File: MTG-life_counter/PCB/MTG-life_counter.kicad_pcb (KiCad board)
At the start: 2 copper layers, 65 x 43 mm, 51 parts, among them J1 USB_C_Receptacle, J2 AVR-ISP-6, Q1 IRLML6244, Q2 Si2301DS, Q3 Si2301DS, SW1 SW_Push, SW2 SW_Push, U1 MCP73831-2-OT, U2 AT90S4433-8P, U3 HDSP-H101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

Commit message: USB C connector placed and routed.
This fixes #6.
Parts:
- added D3: S1B, Diode_SMD:D_SMA_Handsoldering, B.Cu at (123.5, 120.2)
- moved C4 41.3 mm to (125.5, 110.6), turned to 180 degrees
- moved D1 30.8 mm to (132.5, 110.6), turned to 0 degrees
- moved R16 23.8 mm to (139.2, 103.7)
- moved R20 23.0 mm to (139.2, 105.7)
- moved D2 20.6 mm to (145.0, 103.6), turned to 180 degrees
- moved REF** 17.8 mm to (160.3, 125.9)
- moved R13 17.2 mm to (143.7, 106.3), turned to 180 degrees
- moved J1 16.0 mm to (132.5, 106.5)
- moved REF** 15.4 mm to (149.4, 108.8)
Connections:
- net Net-(J1-PadA5) renamed /Power/CC1
- net Net-(J1-PadB5) renamed /Power/CC2
- J2 pad 2: +BATT -> Net-(D3-Pad2)
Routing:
- net /Power/VUSB: track 96.5 -> 67.3 mm
- net +BATT: track 92.3 -> 71.6 mm
- net /Power/CHARGER_STAT: track 43.1 -> 26.0 mm
- net /Power/CC1: track 0.00 -> 7.46 mm
- net /Power/CC2: track 0.00 -> 7.12 mm
- net GND: track 26.8 -> 33.3 mm
- net Net-(D3-Pad2): track 0.00 -> 5.96 mm
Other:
- board text added: "+BTN"
- board text added: "-BTN"
- board text added: "Battery"
- board text added: "Charging"
- board text added: "Rev. 22/2"
- board text removed: "Rev. 22/1"

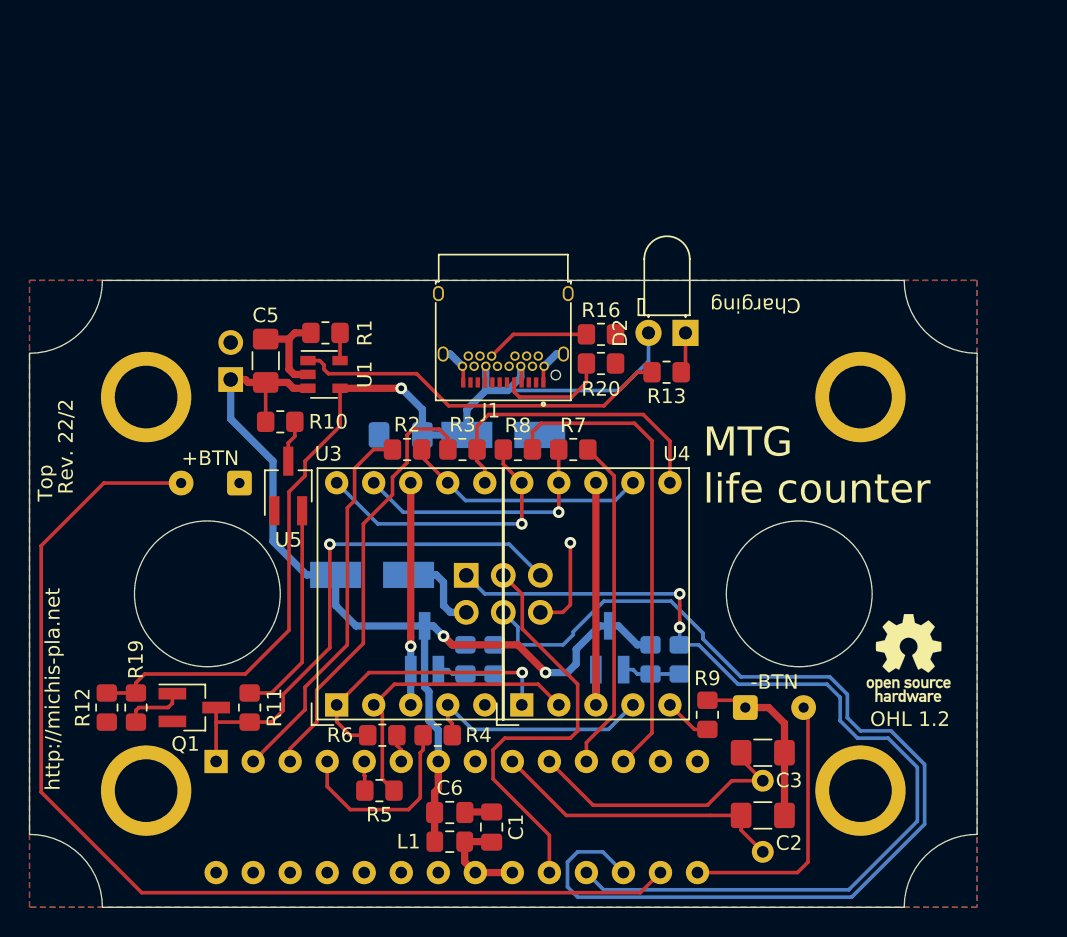
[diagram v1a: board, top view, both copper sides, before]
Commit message: Add an on/off switch. This fixes #7.
Also fix ERC errors, rename nets to indicate the signals logic level, move some components a bit and update BOM & netlist.

This is rev. 22/2 of the board.
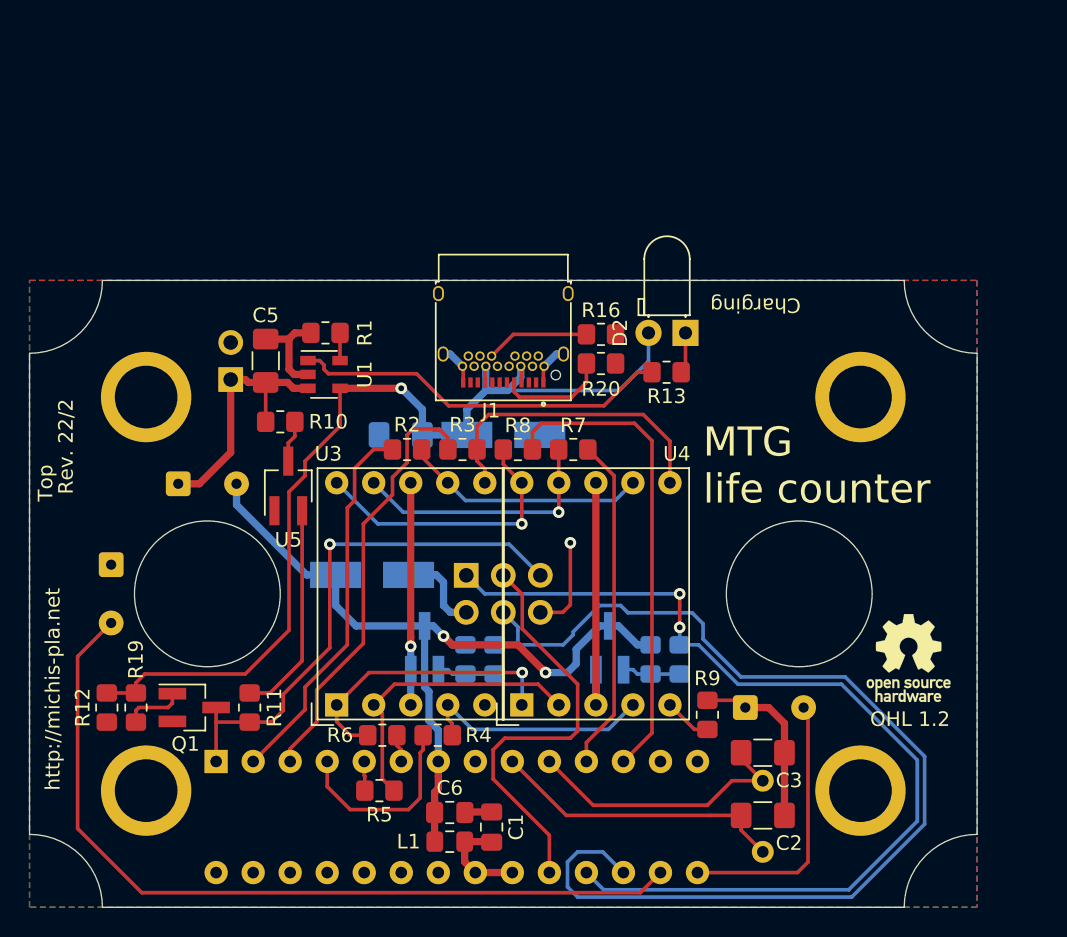
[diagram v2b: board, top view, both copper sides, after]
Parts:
- added SW3: SW_SPST, Connector_Wire:SolderWire-0.15sqmm_1x02_P4mm_D0.5mm_OD1.5mm, F.Cu at (110.2, 114.0)
- moved SW2 10.4 mm to (105.6, 119.5), turned to 270 degrees
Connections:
- net /SW_DEC renamed /~SW_DEC
- net /SW_INC renamed /~SW_INC
- C6 pad 1: +BATT -> +3V8
- D3 pad 1: +BATT -> +3V8
- L1 pad 1: +BATT -> +3V8
- Q2 pad 3: +BATT -> +3V8
- Q3 pad 3: +BATT -> +3V8
- R17 pad 1: +BATT -> +3V8
- R18 pad 1: +BATT -> +3V8
- U2 pad 7: +BATT -> +3V8
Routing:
- net +3V8: track 0.00 -> 56.1 mm, vias 0 -> 2
- net +BATT: track 71.6 -> 17.7 mm, vias 2 -> 0
- net /~SW_INC: track 74.2 -> 57.4 mm
- net /~DIGIT_2_ENABLE: track 51.3 -> 50.6 mm
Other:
- board text added: "On/off switch"
